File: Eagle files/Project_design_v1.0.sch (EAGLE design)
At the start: 11 parts, among them U1 MCP9700T-E/TT

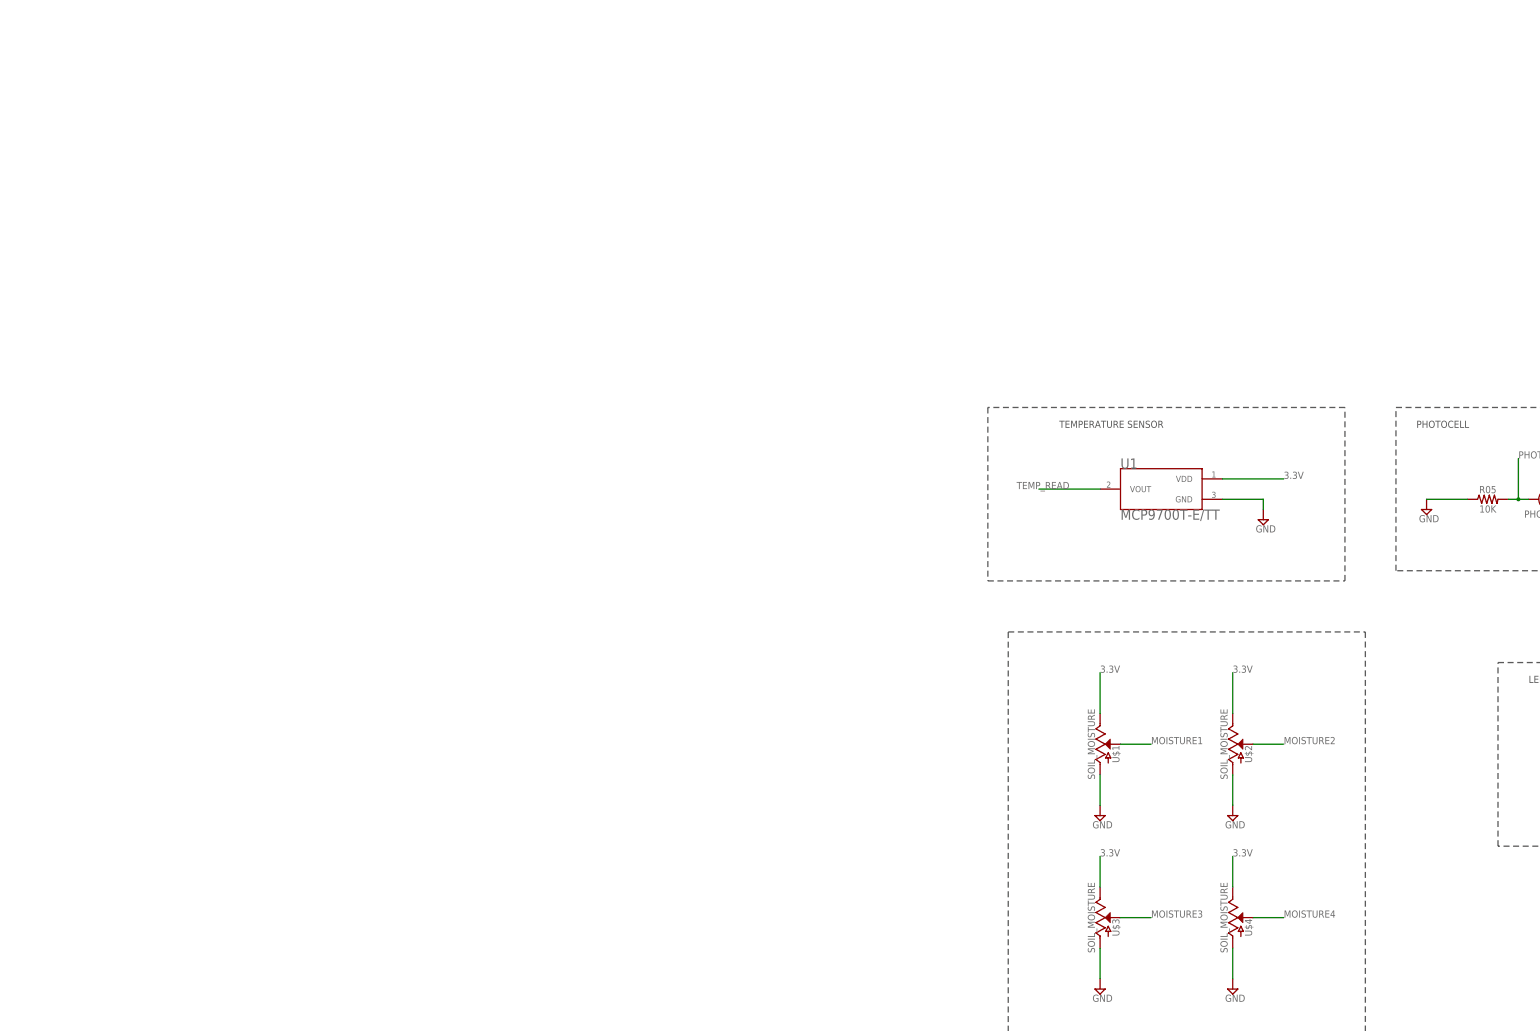
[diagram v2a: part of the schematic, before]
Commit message: MCU, charging IC & power supply implemented on the eagle schematics
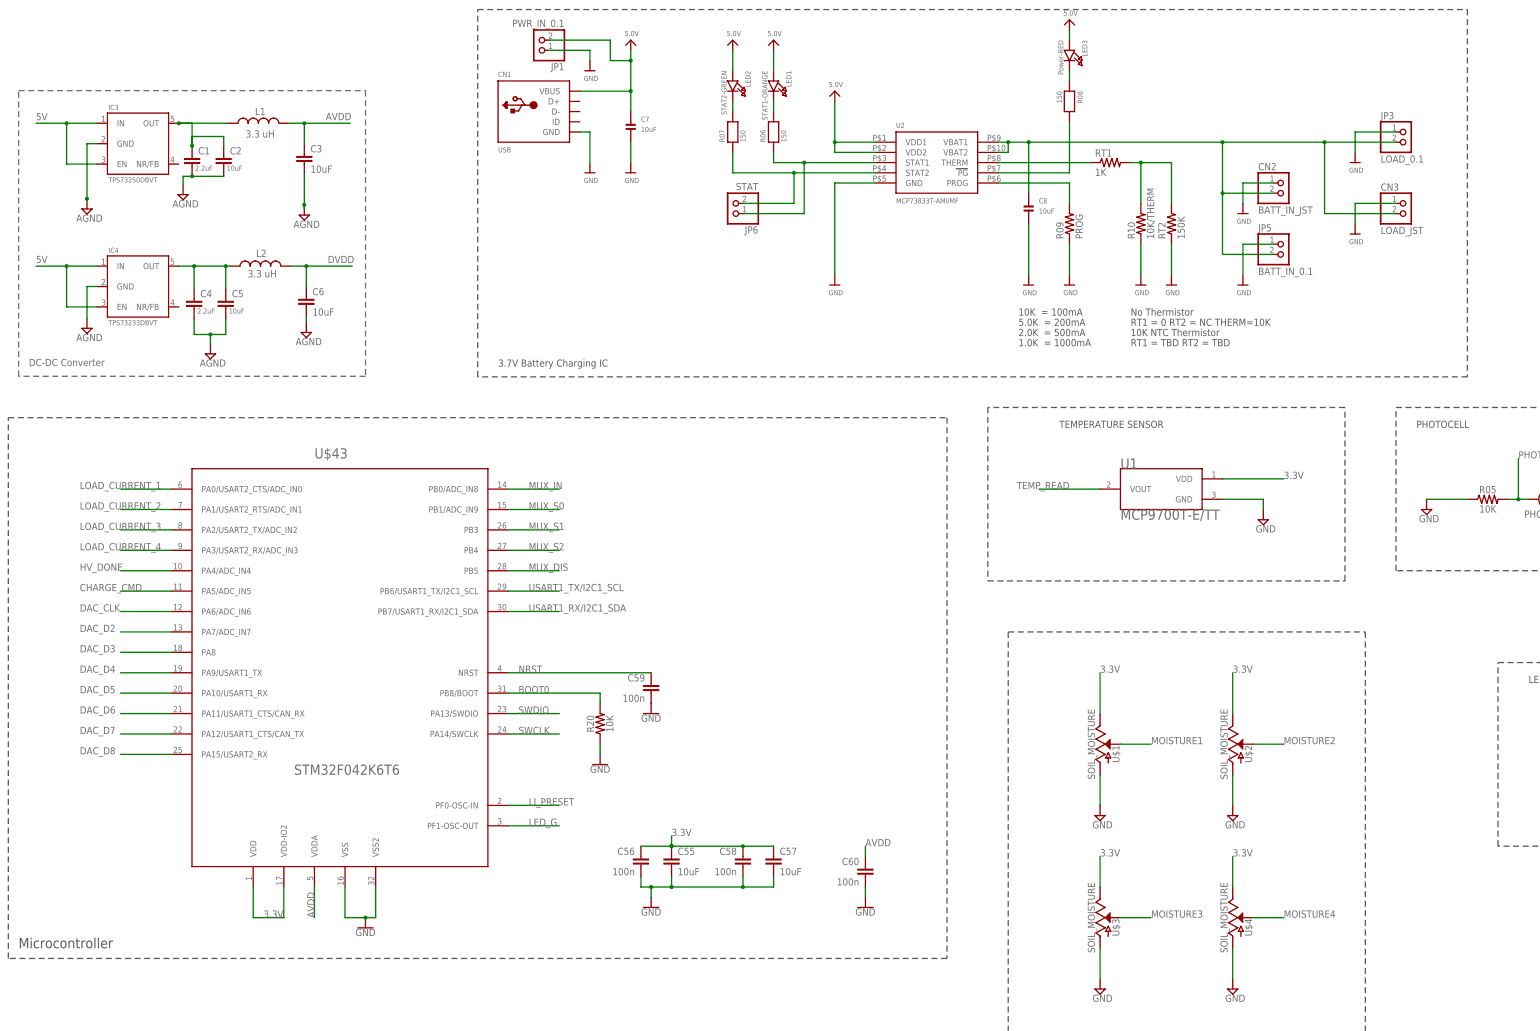
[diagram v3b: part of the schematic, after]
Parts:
- added C1, C4: 2.2uF, SparkFun-Passives:CAP0603-CAP
- added C2, C3, C5, C6: 10uF, SparkFun-Passives:CAP0603-CAP
- added C55, C57: 10uF, custom_part:CAPA1206
- added C56, C58, C59, C60: 100n, custom_part:CAPA0402
- added C7, C8: 10uF, microbuilder:CAP_CERAMIC0805
- added CN1: USB, microbuilder:USBMINIBLARGE
- added CN2: BATT_IN_JST, microbuilder:JST_2PIN
- added CN3: LOAD_JST, microbuilder:JST_2PIN
- added IC3: TPS73250DBVT, TPS32xx:TPS732XXDBV
- added IC4: TPS73233DBVT, TPS32xx:TPS732XXDBV
- added JP1: PWR_IN_0.1, microbuilder:HEADER-1X2
- added JP3: LOAD_0.1, microbuilder:HEADER-1X2
- added JP5: BATT_IN_0.1, microbuilder:HEADER-1X2
- added JP6: STAT, microbuilder:HEADER-1X2
- added L1, L2: 3.3 uH, SparkFun-Passives:INDUCTOR0603
- added LED1: STAT1-ORANGE, microbuilder:LED0805
- added LED2: STAT2-GREEN, microbuilder:LED0805
- added LED3: Power-RED, microbuilder:LED0805
- added R06, R07, R08: 150, microbuilder:RESISTOR0805
- added R09: PROG, microbuilder:RESISTOR_DUAL
- added R10: 10K/THERM, adafruit:R-US_FLIPFLOP
- added R20: 10K, custom_part:0603RESIST
- added RT1: 1K, adafruit:R-US_R0805
- added RT2: 150K, adafruit:R-US_R0805
- added U$43: STM32F042K6T6, stm32-microcontrollers:STM32F042K6T6
- added U2: MCP73833T-AMI/MF, microbuilder:MCP73833DFN
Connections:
- new net 5.0V: C7.P$1, CN1.VBUS, JP1.2, LED1.A, LED2.A, LED3.A, U2.VDD1, U2.VDD2
- new net 5V: IC3.EN, IC3.IN, IC4.EN, IC4.IN
- new net AGND: C1.2, C2.2, C3.2, C4.2, C5.2, C6.2, IC3.GND, IC4.GND
- new net AVDD: C3.1, C60.1, L1.2, U$43.VDDA
- new net BATT: C8.P$1, CN2.2, CN3.2, JP3.2, JP5.2, U2.VBAT1, U2.VBAT2
- new net BOOT0: R20.2, U$43.PB8/BOOT
- new net CHARGE_CMD: U$43.PA5/ADC_IN5
- new net DAC_CLK: U$43.PA6/ADC_IN6
- new net DAC_D2: U$43.PA7/ADC_IN7
- new net DAC_D3: U$43.PA8
- new net DAC_D4: U$43.PA9/USART1_TX
- new net DAC_D5: U$43.PA10/USART1_RX
- new net DAC_D6: U$43.PA11/USART1_CTS/CAN_RX
- new net DAC_D7: U$43.PA12/USART1_CTS/CAN_TX
- new net DAC_D8: U$43.PA15/USART2_RX
- new net DVDD: C6.1, L2.2
- new net HV_DONE: U$43.PA4/ADC_IN4
- new net LI_PRESET: U$43.PF0-OSC-IN
- new net LOAD_CURRENT_1: U$43.PA0/USART2_CTS/ADC_IN0
- new net LOAD_CURRENT_2: U$43.PA1/USART2_RTS/ADC_IN1
- new net LOAD_CURRENT_3: U$43.PA2/USART2_TX/ADC_IN2
- new net LOAD_CURRENT_4: U$43.PA3/USART2_RX/ADC_IN3
- new net MUX_DIS: U$43.PB5
- new net MUX_IN: U$43.PB0/ADC_IN8
- new net MUX_S0: U$43.PB1/ADC_IN9
- new net MUX_S1: U$43.PB3
- new net MUX_S2: U$43.PB4
- new net N$12: LED3.C, R08.1
- new net N$13: C1.1, C2.1, IC3.OUT, L1.1
- new net N$16: R09.2, U2.PROG
- new net N$2: C4.1, C5.1, IC4.OUT, L2.1
- new net N$3: LED1.C, R06.2
- new net N$4: LED2.C, R07.2
- new net N$5: JP6.1, R06.1, U2.STAT1
- new net N$6: JP6.2, R07.1, U2.STAT2
- new net N$7: R08.2, U2.PG
- new net N$8: RT1.1, U2.THERM
- new net N$9: R10.2, RT1.2, RT2.2
- new net NRST: C59.1, U$43.NRST
- new net SWCLK: U$43.PA14/SWCLK
- new net SWDIO: U$43.PA13/SWDIO
- new net USART1_RX/I2C1_SDA: U$43.PB7/USART1_RX/I2C1_SDA
- new net USART1_TX/I2C1_SCL: U$43.PB6/USART1_TX/I2C1_SCL
- net 3.3V: now also C55.1, C56.1, C57.1, C58.1, U$43.VDD, U$43.VDD-IO2
- net GND: now also C55.2, C56.2, C57.2, C58.2, C59.2, C60.2, C7.P$2, C8.P$2, CN1.GND, CN2.1, CN3.1, JP1.1, JP3.1, JP5.1, R09.1, R10.1, R20.1, RT2.1, U$43.VSS, U$43.VSS2, U2.GND
- net LED_G: now also U$43.PF1-OSC-OUT
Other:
- note added: "1.0K = 1000mA"
- note added: "10K = 100mA"
- note added: "10K NTC Thermistor"
- note added: "2.0K = 500mA"
- note added: "3.7V Battery Charging IC"
- note added: "5.0K = 200mA"
- note added: "Bypassing Capacitor Analog + Digital"
- note added: "DC-DC Converter"
- note added: "Microcontroller"
- note added: "No Thermistor"
- note added: "RT1 = 0 RT2 = NC THERM=10K"
- note added: "RT1 = TBD RT2 = TBD"

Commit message: corrections of few wire in the schematics
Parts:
- removed CN3: LOAD_JST, microbuilder:JST_2PIN
- removed JP6: STAT, microbuilder:HEADER-1X2
- added C9: 100n, custom_part:CAPA0402
- added D1, D2, D3, D8: (no value), adafruit:DIODEDO-1N4148
- added JP2: MOTOR2, microbuilder:HEADER-1X2
- added JP4: MOTOR3, microbuilder:HEADER-1X2
- added U$16, U$19, U$20, U$23: PMV16XN, custom_part_2:PMV16XN
- IC1: value TPS73250DBVT -> TPS73233DBVT; PARTNO TPS73250DBVT -> TPS73233DBVT
- JP1: value PWR_IN_0.1 -> MOTOR1
- JP5: value BATT_IN_0.1 -> MOTOR4
- renumbered IC3 to IC1
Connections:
- removed net 5V: IC1.EN, IC1.IN, IC4.EN, IC4.IN
- removed net AVDD: C3.1, C60.1, L1.2, U$43.VDDA
- removed net BATT: C8.P$1, CN2.2, CN3.2, JP3.2, JP5.2, U2.VBAT1, U2.VBAT2
- removed net DVDD: C6.1, L2.2
- new net CTRL_MOIST1: U$1.VCC
- new net CTRL_MOIST2: U$2.VCC
- new net CTRL_MOIST3: U$3.VCC
- new net CTRL_MOIST4: U$4.VCC
- new net CTRL_MOTOR1: U$16.G
- new net CTRL_MOTOR2: U$19.G
- new net CTRL_MOTOR3: U$20.G
- new net CTRL_MOTOR4: U$23.G
- new net CTRL_PHOTOCELL: R04.P$2
- new net N$10: D8.A, JP1.2, U$16.D
- new net N$11: D1.A, JP2.2, U$19.D
- new net N$14: D2.A, JP4.2, U$20.D
- new net N$15: D3.A, JP5.2, U$23.D
- new net VCC: C3.1, C60.1, D1.C, D2.C, D3.C, D8.C, JP1.1, JP2.1, JP4.1, JP5.1, L1.2, U$43.VDDA
- new net V_BAT: C8.P$1, CN2.2, IC1.EN, IC1.IN, IC4.EN, IC4.IN, JP3.2, U2.VBAT1, U2.VBAT2
- net 3.3V: now also C6.1, L2.2; no longer R04.P$2, U$1.VCC, U$2.VCC, U$3.VCC, U$4.VCC
- net 5.0V: now also C9.1; no longer JP1.2
- net GND: now also C9.2, U$16.S, U$19.S, U$20.S, U$23.S; no longer CN3.1, JP1.1, JP5.1
- net N$5: no longer JP6.1
- net N$6: no longer JP6.2
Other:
- note added: "Motor control"
- note added: "charge/done"
- note added: "find a RGB LED with common cathode instead of common anode"
- note added: "pwr"
- moved on the sheet: C7, CN1, CN2, JP1, JP3, JP5, LD1, LED1, LED2, LED3, R01, R02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

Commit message: part number & potentiometer to select the ammount of water needed for each pot
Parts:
- removed C55, C57: 10uF, custom_part:CAPA1206
- removed D8: (no value), adafruit:DIODEDO-1N4148
- removed LED1: STAT1-ORANGE, microbuilder:LED0805
- removed LED2: STAT2-GREEN, microbuilder:LED0805
- removed LED3: Power-RED, microbuilder:LED0805
- removed RT1: 1K, adafruit:R-US_R0805
- removed RT2: 150K, adafruit:R-US_R0805
- removed U$1, U$2, U$3, U$4: SOIL_MOISTURE, potentiometer:SOIL_MOISTURE
- removed U$16, U$19, U$20, U$23: PMV16XN, custom_part_2:PMV16XN
- removed U$43: STM32F042K6T6, stm32-microcontrollers:STM32F042K6T6
- removed U1: MCP9700T-E/TT, MCP9700T-E_TT:MCP9700T-E/TT
- removed U2: MCP73833T-AMI/MF, microbuilder:MCP73833DFN
- added C10, C11, C12: 100n, custom_part:CAPA0402
- added D4: 1N4148W, diode:CGRM4002-G
- added H1, H2, H3, H4, H5, H6, H7, H8: SOIL_MOISTURE, potentiometer:SOIL_MOISTURE
- added IC2: TPS73233DBVT, TPS32xx:TPS732XXDBV
- added IC3: MCP73833T-AMI/MF, microbuilder:MCP73833DFN
- added IC5: MCP9700T-E/TT, MCP9700T-E_TT:MCP9700T-E/TT
- added IC6: TLV379IDBVT, AD8009JRTZ-REEL:AD8009JRTZ-REEL
- added JP6: Contact_pin, microbuilder:HEADER-1X2
- added LD2: RGB_LED, Semicond:ASMB-MTB0-0A3A2PLCC-4
- added LD3: RLED, LTST-C190KRKT:LTST-C190KRKT
- added Q1, Q2, Q3, Q4: PMV16XN, custom_part_2:PMV16XN
- added R11, R12: 221, custom_part:0603RESIST
- C7: device microbuilder:CAP_CERAMIC0805 -> SparkFun-Passives:CAP0603-CAP; PARTNO (none) -> GRM188R60J106ME47D
- C8: value 10uF -> 100n; device microbuilder:CAP_CERAMIC0805 -> custom_part:CAPA0402; PARTNO (none) -> CGA2B3X7R1E104K050BB
- CN1: value USB -> USB_CONN; device microbuilder:USBMINIBLARGE -> 105133-0011:105133-0011; PARTNO (none) -> 105133-0011
- CN2: PARTNO (none) -> B2B-XH-A(LF)(SN)
- D1, D2, D3: value (none) -> 1N4148W; device adafruit:DIODEDO-1N4148 -> diode:CGRM4002-G; PARTNO (none) -> 1N4148W
- IC4: value TPS73233DBVT -> STM32F042K6T6; device TPS32xx:TPS732XXDBV -> stm32-microcontrollers:STM32F042K6T6; PARTNO TPS73233DBVT -> STM32F042K6T6
- JP1: value MOTOR1 -> Contact_pin
- JP2: value MOTOR2 -> Contact_pin
- JP3: value LOAD_0.1 -> Contact_pin
- JP4: value MOTOR3 -> Contact_pin
- JP5: value MOTOR4 -> Contact_pin
- LD1: value ASMB-MTB0-0A3A2PLCC-4 -> RGB_LED
- R01: value 3K -> 2k
- R02, R03: value 2K -> 2k
- R04: PARTNO (none) -> 1528-2141-ND
- R05: value 10K -> 10k
- R06, R07, R08: value 150 -> 221; device microbuilder:RESISTOR0805 -> custom_part:0603RESIST; PARTNO (none) -> ERJ-PA3F2210V
- R09: value PROG -> 2k; device microbuilder:RESISTOR_DUAL -> custom_part:0603RESIST; PARTNO (none) -> ERJ-PA3F2001V
- R10: value 10K/THERM -> 10k; device adafruit:R-US_FLIPFLOP -> custom_part:0603RESIST; PARTNO (none) -> ERJ-PA3F1002V
- R20: value 10K -> 10k; PARTNO ERJ-3EKF4020V -> ERJ-PA3F1002V
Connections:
- removed net AGND: C1.2, C2.2, C3.2, C4.2, C5.2, C6.2, IC1.GND, IC4.GND
- removed net N$9: R10.2, RT1.2, RT2.2
- new net LEVEL_SENSOR: JP6.1
- new net N$17: IC6.+IN, R11.1, R12.2
- new net V_BAT_SENSE: IC6.-IN, IC6.VOUT
- new net WATER_ADJ_1: H5.VOUT
- new net WATER_ADJ_2: H6.VOUT
- new net WATER_ADJ_3: H7.VOUT
- new net WATER_ADJ_4: H8.VOUT
- net 3.3V: now also C10.1, C11.1, C12.1, H5.VCC, H6.VCC, H7.VCC, H8.VCC, IC4.VDD, IC4.VDD-IO2, IC5.VDD, IC6.+VS; no longer C55.1, C57.1, U$43.VDD, U$43.VDD-IO2, U1.VDD
- net 5.0V: now also C7.1, IC3.VDD1, IC3.VDD2, LD2.1, LD3.A; no longer C7.P$1, LED1.A, LED2.A, LED3.A, U2.VDD1, U2.VDD2
- net BOOT0: now also IC4.PB8/BOOT; no longer U$43.PB8/BOOT
- net CHARGE_CMD: now also IC4.PA5/ADC_IN5; no longer U$43.PA5/ADC_IN5
- net CTRL_MOIST1: now also H1.VCC; no longer U$1.VCC
- net CTRL_MOIST2: now also H2.VCC; no longer U$2.VCC
- net CTRL_MOIST3: now also H3.VCC; no longer U$3.VCC
- net CTRL_MOIST4: now also H4.VCC; no longer U$4.VCC
- net CTRL_MOTOR1: now also Q1.G; no longer U$16.G
- net CTRL_MOTOR2: now also Q2.G; no longer U$19.G
- net CTRL_MOTOR3: now also Q3.G; no longer U$20.G
- net CTRL_MOTOR4: now also Q4.G; no longer U$23.G
- net DAC_CLK: now also IC4.PA6/ADC_IN6; no longer U$43.PA6/ADC_IN6
- net DAC_D2: now also IC4.PA7/ADC_IN7; no longer U$43.PA7/ADC_IN7
- net DAC_D3: now also IC4.PA8; no longer U$43.PA8
- net DAC_D4: now also IC4.PA9/USART1_TX; no longer U$43.PA9/USART1_TX
- net DAC_D5: now also IC4.PA10/USART1_RX; no longer U$43.PA10/USART1_RX
- net DAC_D6: now also IC4.PA11/USART1_CTS/CAN_RX; no longer U$43.PA11/USART1_CTS/CAN_RX
- net DAC_D7: now also IC4.PA12/USART1_CTS/CAN_TX; no longer U$43.PA12/USART1_CTS/CAN_TX
- net DAC_D8: now also IC4.PA15/USART2_RX; no longer U$43.PA15/USART2_RX
- net GND: now also C1.2, C10.2, C11.2, C12.2, C2.2, C3.2, C4.2, C5.2, C6.2, C7.2, C8.2, CN1.SHIELD, H1.GND, H2.GND, H3.GND, H4.GND, H5.GND, H6.GND, H7.GND, H8.GND, IC1.GND, IC2.GND, IC3.GND, IC4.VSS, IC4.VSS2, IC5.GND, IC6.-VS, JP1.1, JP6.2, Q1.S, Q2.S, Q3.S, Q4.S, R12.1; no longer C55.2, C57.2, C7.P$2, C8.P$2, JP3.1, RT2.1, U$1.GND, U$16.S, U$19.S, U$2.GND, U$20.S, U$23.S, U$3.GND, U$4.GND, U$43.VSS, U$43.VSS2, U1.GND, U2.GND
- net HV_DONE: now also IC4.PA4/ADC_IN4; no longer U$43.PA4/ADC_IN4
- net LED_G: now also IC4.PF1-OSC-OUT; no longer U$43.PF1-OSC-OUT
- net LI_PRESET: now also IC4.PF0-OSC-IN; no longer U$43.PF0-OSC-IN
- net LOAD_CURRENT_1: now also IC4.PA0/USART2_CTS/ADC_IN0; no longer U$43.PA0/USART2_CTS/ADC_IN0
- net LOAD_CURRENT_2: now also IC4.PA1/USART2_RTS/ADC_IN1; no longer U$43.PA1/USART2_RTS/ADC_IN1
- net LOAD_CURRENT_3: now also IC4.PA2/USART2_TX/ADC_IN2; no longer U$43.PA2/USART2_TX/ADC_IN2
- net LOAD_CURRENT_4: now also IC4.PA3/USART2_RX/ADC_IN3; no longer U$43.PA3/USART2_RX/ADC_IN3
- net MOISTURE1: now also H1.VOUT; no longer U$1.VOUT
- net MOISTURE2: now also H2.VOUT; no longer U$2.VOUT
- net MOISTURE3: now also H3.VOUT; no longer U$3.VOUT
- net MOISTURE4: now also H4.VOUT; no longer U$4.VOUT
- net MUX_DIS: now also IC4.PB5; no longer U$43.PB5
- net MUX_IN: now also IC4.PB0/ADC_IN8; no longer U$43.PB0/ADC_IN8
- net MUX_S0: now also IC4.PB1/ADC_IN9; no longer U$43.PB1/ADC_IN9
- net MUX_S1: now also IC4.PB3; no longer U$43.PB3
- net MUX_S2: now also IC4.PB4; no longer U$43.PB4
- net N$10: now also D4.A, JP2.2, Q1.D; no longer D8.A, JP1.2, U$16.D
- net N$11: now also JP3.2, Q2.D; no longer JP2.2, U$19.D
- net N$12: now also LD3.C, R08.2; no longer LED3.C, R08.1
- net N$14: now also Q3.D; no longer U$20.D
- net N$15: now also Q4.D; no longer U$23.D
- net N$16: now also IC3.PROG; no longer U2.PROG
- net N$2: now also IC2.OUT; no longer IC4.OUT
- net N$3: now also LD2.3; no longer LED1.C
- net N$4: now also LD2.4; no longer LED2.C
- net N$5: now also IC3.STAT1, R07.1; no longer R06.1, U2.STAT1
- net N$6: now also IC3.STAT2, R06.1; no longer R07.1, U2.STAT2
- net N$7: now also IC3.PG, R08.1; no longer R08.2, U2.PG
- net N$8: now also IC3.THERM, R10.2; no longer RT1.1, U2.THERM
- net NRST: now also IC4.NRST; no longer U$43.NRST
- net SWCLK: now also IC4.PA14/SWCLK; no longer U$43.PA14/SWCLK
- net SWDIO: now also IC4.PA13/SWDIO; no longer U$43.PA13/SWDIO
- net TEMP_READ: now also IC5.VOUT; no longer U1.VOUT
- net USART1_RX/I2C1_SDA: now also IC4.PB7/USART1_RX/I2C1_SDA; no longer U$43.PB7/USART1_RX/I2C1_SDA
- net USART1_TX/I2C1_SCL: now also IC4.PB6/USART1_TX/I2C1_SCL; no longer U$43.PB6/USART1_TX/I2C1_SCL
- net VCC: now also D4.C, IC4.VDDA, JP3.1; no longer D8.C, JP1.1, U$43.VDDA
- net V_BAT: now also C8.1, IC2.EN, IC2.IN, IC3.VBAT1, IC3.VBAT2, JP1.2, R11.2; no longer C8.P$1, IC4.EN, IC4.IN, JP3.2, U2.VBAT1, U2.VBAT2
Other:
- note added: "ERJ-3EKF1002V"
- note added: "ERJ-3EKF2210V"
- note added: "Level Sensor"
- note added: "V_bat monitoring"
- note added: "Watering Adjustement"
- moved on the sheet: C1, C2, C3, C4, C5, C56, C58, C6, C60, C7, C8, C9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
